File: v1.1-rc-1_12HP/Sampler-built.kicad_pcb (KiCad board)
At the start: 2 copper layers, 173.5 x 198.7 mm, 267 parts, among them J10 Eurorack_Power_10pin_Unshroud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, J11 3.5mm_Mono_Switched, J12 3.5mm_Mono_Switched, J13 3.5mm_Mono_Switched, J14 3.5mm_Mono_Switched, J15 3.5mm_Mono_Switched, J16 3.5mm_Mono_Switched, J17 3.5mm_Mono_Switched, J2 3.5mm_Mono_Switched, J3 Conn_01x04, J4 Conn_02x04, J6 3.5mm_Mono_Switched, J7 3.5mm_Mono_Switched, J8 3.5mm_Mono_Switched, J9 3.5mm_Mono_Switched, U1 TL072H, U10 TL072H, U11 TL072H, U12 TL072H, U13 AP62200WU-7, U15 NJM2068, U16 NJM2068, U17 AZ1117CR-3.3TRG1, U2 STM32F746IE, U3 TL072H, U4 SDRAM_IS42S16400J-6BLI-TR, U5 TL072H, U6 NCP51460SN33, U7 TL072H, U8 TL072H, U9 PCM3060PW, Y1 16MHz_18pF_FA238

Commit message: v1.1-rc1-12HP: part placement and routing ip
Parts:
- removed C16, C20: 10nF_0402_16V, 4ms_Capacitor:C_0402
- removed C89: 18pF_0603_50V, 4ms_Capacitor:C_0603
- removed C91, C92, C93, C94, C95, C96: 100nF_0402_16V, 4ms_Capacitor:C_0402
- removed D10, D11, D12, D13, D14, D18, D2, D27, D28, D30, D31, D32, D4, D5, D6, D8, D9: BAT54S, 4ms_Package_SOT:SOT23-3_PO132
- removed R31: 3k_0402, 4ms_Resistor:R_0402
- removed R37: 68Ω_0402, 4ms_Resistor:R_0402
- removed R38: 10k_0603, 4ms_Resistor:R_0603
- removed R39: 2k_0402, 4ms_Resistor:R_0402
- removed R69, R72: 1k_0603, 4ms_Resistor:R_0603
- removed R76: 47k_0603, 4ms_Resistor:R_0603
- removed S1, S2: SW_Push_PTS526 SM15 SMTR2 LFS, 4ms_Switch:Button_Tact_PTS526
- removed U17: AZ1117CR-3.3TRG1, 4ms_Package_SOT:SOT89-3
- removed U7: TL072H, 4ms_Package_SSOP:TSSOP-8_4.4x3mm_Pitch0.65mm
- added U14: TL072H, 4ms_Package_SSOP:TSSOP-8_4.4x3mm_Pitch0.65mm, F.Cu at (167.2, 66.8)
- C1, C10, C11, C13, C14, C17, C18, C3, C53, C7, C9: value 0.1uF_0603_16V -> 100nF_0402_16V; footprint 4ms_Capacitor:C_0603 -> 4ms_Capacitor:C_0402
- C12: value 100pF_0603_50V -> 100nF_0402_16V; footprint 4ms_Capacitor:C_0603 -> 4ms_Capacitor:C_0402
- C147, C148, C149, C150, C152, C153, C19, C34, C44, C45, C48, C52, C58, C59, C60, C61, C62, C63, C64, C67, C68, C69, C70, C71, C72, C73, C74, C75, C76, C77, C78, C8, C82, D1, D15, D22, D24, D26, D7, L1, R1, R10, R11, R12, R14, R152, R153, R157, R158, R159, R160, R161, R162, R163, R164, R18, R19, R2, R22, R23, R27, R28, R30, R33, R34, R40, R41, R42, R43, R44, R45, R46, R49, R50, R51, R52, R53, R54, R55, R6, R65, R66, R67, R7, U1, U10, U11, U12, U13, U3, U5, U8: moved to F.Cu
- C2: value 0.1uF_0603_16V -> 2.2uF_0603_25V
- C21, C24: value 100nF_0402_16V -> 47uF_5x5.3_16V; footprint 4ms_Capacitor:C_0402 -> 4ms_Capacitor:CP_Elec_5x5.3; moved to F.Cu
- C23: value 2.2uF_0603_25V -> 18pF_0603_50V
- C25, C26: value 2.2uF_0603_25V -> 0.1uF_0603_16V; moved to F.Cu
- C35, C37: value 100nF_0402_16V -> 100nF_0402_50V
- C38, C40: value 100nF_0402_16V -> 100nF_0402_50V; moved to F.Cu
- C39, C47: value 10nF_0402_16V -> 0.1uF_0603_16V; footprint 4ms_Capacitor:C_0402 -> 4ms_Capacitor:C_0603; moved to F.Cu
- C4, C5: value 47uF_5x5.3_16V -> 2.2uF_0603_25V; footprint 4ms_Capacitor:CP_Elec_5x5.3 -> 4ms_Capacitor:C_0603
- C42: value 100nF_0402_16V -> 0.1uF_0603_16V; footprint 4ms_Capacitor:C_0402 -> 4ms_Capacitor:C_0603; moved to F.Cu
- C43: value 1uF_0603_25V -> 4.7uF_1206_lowESR; footprint 4ms_Capacitor:C_0603 -> 4ms_Capacitor:C_1206
- C46: value 4.7uF_1206_lowESR -> 1nF_0603_50V; footprint 4ms_Capacitor:C_1206 -> 4ms_Capacitor:C_0603; moved to F.Cu
- C50: value 2.2uF_0603_25V -> 100nF_0402_16V; footprint 4ms_Capacitor:C_0603 -> 4ms_Capacitor:C_0402
- C6: value 1nF_0603_50V -> 100nF_0402_16V; footprint 4ms_Capacitor:C_0603 -> 4ms_Capacitor:C_0402
- C65, C66: value 100nF_0402_50V -> 0.1uF_0603_16V; footprint 4ms_Capacitor:C_0402 -> 4ms_Capacitor:C_0603; moved to F.Cu
- C79: value 100nF_0402_16V -> 0.1uF_0603_16V; footprint 4ms_Capacitor:C_0402 -> 4ms_Capacitor:C_0603
- C83: value 10nF_0402_16V -> 0.1uF_0603_16V; footprint 4ms_Capacitor:C_0402 -> 4ms_Capacitor:C_0603
- C84: value 10nF_0402_16V -> 100pF_0603_50V; footprint 4ms_Capacitor:C_0402 -> 4ms_Capacitor:C_0603
- C87, C88: value 10nF_0402_16V -> 100nF_0402_50V
- R13, R35, R5: value 2k_0402 -> 2k_0603; footprint 4ms_Resistor:R_0402 -> 4ms_Resistor:R_0603; moved to F.Cu
- R29: value 10k_0603 -> 20k_0603
- R3: value 2k_0402 -> 2k_0603; footprint 4ms_Resistor:R_0402 -> 4ms_Resistor:R_0603
- R36: value 10k_0402 -> 10k_0603; footprint 4ms_Resistor:R_0402 -> 4ms_Resistor:R_0603; moved to F.Cu
- R4: value 1k_0603 -> 3k_0402; footprint 4ms_Resistor:R_0603 -> 4ms_Resistor:R_0402
- R64, R68: value 1k_0603 -> 2k_0603
- R9: value 2k_0402 -> 1k_0603; footprint 4ms_Resistor:R_0402 -> 4ms_Resistor:R_0603; moved to F.Cu
- moved C90 250.7 mm to (169.5, 102.4)
- moved C57 247.6 mm to (163.1, 104.2), turned to 90 degrees
- moved R57 242.9 mm to (169.9, 83.1), turned to -90 degrees
- moved R56 242.6 mm to (169.9, 79.7), turned to -90 degrees
- moved R29 240.1 mm to (167.3, 82.1)
- moved C87 235.5 mm to (168.8, 64.2), turned to 180 degrees
- moved R32 234.5 mm to (164.4, 76.5)
- moved R60 234.1 mm to (148.8, 116.4), turned to -90 degrees
- moved C97 232.9 mm to (170.0, 69.9), turned to -90 degrees
- moved C88 231.3 mm to (165.8, 64.2)
- moved U15 231.2 mm to (165.0, 79.4)
- moved R61 230.9 mm to (148.8, 112.1), turned to 90 degrees
- moved C84 230.2 mm to (146.2, 112.5), turned to 180 degrees
- moved R63 229.7 mm to (143.6, 111.5), turned to 90 degrees
- moved R62 226.9 mm to (146.2, 110.8), turned to 180 degrees
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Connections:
- net +5VA renamed +5V
- net Net-(U2A-BOOT) renamed /BOOT0
- net Net-(U2A-NRST) renamed /NRST
- C1 pad 1: Net-(D9-AK) -> +3V3
- C1 pad 2: GNDADC -> GND
- C10 pad 1: +12V -> +3V3
- C11 pad 1: -12VA -> +3V3
- C12 pad 1: Net-(U16A--) -> +3V3
- C12 pad 2: Net-(C12-Pad2) -> GND
- C13 pad 1: +12V -> +3V3
- C14 pad 1: -12VA -> +3V3
- C17 pad 1: +12V -> +3V3
- C18 pad 1: -12VA -> +3V3
- C19 pad 1: Net-(D7-AK) -> /D2
- C2 pad 1: Net-(POT_SAMP1-Center) -> Net-(U2B-VCAP_2)
- C2 pad 2: GNDADC -> GND
- C21 pad 1: +3V3 -> +12V
- C23 pad 1: Net-(U2B-VCAP_2) -> /OSC_OUT
- C24 pad 1: +3V3 -> GND
- C24 pad 2: GND -> -12VA
- C25 pad 1: Net-(U2B-VCAP_1) -> +12V
- C26 pad 1: GND -> -12VA
- C26 pad 2: Net-(U2B-VDD12OTGHS) -> GND
- C27 pad 1: +3.3VADC -> +3V3
- C27 pad 2: GNDADC -> GND
- C3 pad 1: GND -> +3V3
- C3 pad 2: Net-(U15B-+) -> GND
- C35 pad 1: +3V3 -> +12V
- C37 pad 1: +3V3 -> -12VA
- C38 pad 1: +3V3 -> +12V
- C39 pad 1: Net-(D28-AK) -> /A6
- C4 pad 1: +12V -> Net-(U2B-VCAP_1)
- C40 pad 1: +3V3 -> -12VA
- C42 pad 1: +3V3 -> GND
- C42 pad 2: GND -> Net-(U15B-+)
- C43 pad 1: +12V -> +3V3
- C46 pad 1: +3V3 -> Net-(C46-Pad1)
- C46 pad 2: GND -> Net-(U15B--)
- C47 pad 1: Net-(D32-AK) -> /D6
- C5 pad 2: -12VA -> Net-(U2B-VDD12OTGHS)
- C53 pad 1: /D6 -> +3V3
- C54 pad 1: Net-(C54-Pad1) -> /D12
- C6 pad 1: Net-(C6-Pad1) -> +3.3VADC
- C6 pad 2: Net-(U15B--) -> GNDADC
- C65 pad 1: +12V -> Net-(POT_START1-Center)
- C65 pad 2: GND -> GNDADC
- C66 pad 1: -12VA -> Net-(POT_LENGTH1-Center)
- C66 pad 2: GND -> GNDADC
- C7 pad 1: Net-(POT_LENGTH1-Center) -> +3V3
- C7 pad 2: GNDADC -> GND
- C79 pad 1: +3V3 -> Net-(POT_SAMP1-Center)
- C79 pad 2: GND -> GNDADC
- C83 pad 1: Net-(Bank_But1-G) -> Net-(POT_PITCH1-Center)
- C83 pad 2: GND -> GNDADC
- C84 pad 1: Net-(D10-AK) -> Net-(U16B--)
- C84 pad 2: GND -> Net-(C84-Pad2)
- C87 pad 1: Net-(D18-AK) -> +12V
- C88 pad 1: Net-(D31-AK) -> -12VA
- C9 pad 1: Net-(POT_START1-Center) -> +3V3
- C9 pad 2: GNDADC -> GND
- D7 pad 3: Net-(D7-AK) -> /D2
- J13 pad 3: unconnected-(J13-SW-Pad3) -> GND
- J14 pad 3: unconnected-(J14-SW-Pad3) -> GND
- J4 pad 1: unconnected-(J4-Pin_1-Pad1) -> /UART_TX
- J4 pad 2: unconnected-(J4-Pin_2-Pad2) -> GND
- J4 pad 3: unconnected-(J4-Pin_3-Pad3) -> /UART_RX
- J4 pad 4: unconnected-(J4-Pin_4-Pad4) -> GND
- J4 pad 5: unconnected-(J4-Pin_5-Pad5) -> /DEBUG2
- J4 pad 6: unconnected-(J4-Pin_6-Pad6) -> GND
- J4 pad 7: unconnected-(J4-Pin_7-Pad7) -> /DEBUG3
- J4 pad 8: unconnected-(J4-Pin_8-Pad8) -> GND
- POT_PITCH1 pad 2: Net-(D9-AK) -> Net-(POT_PITCH1-Center)
- R1 pad 1: /A0 -> Net-(R1-Pad1)
- R11 pad 1: /A1 -> Net-(POT_PITCH1-Center)
- R11 pad 2: Net-(D9-AK) -> Net-(U1B-+)
- R12 pad 2: Net-(D9-AK) -> /A1
- R13 pad 2: Net-(D10-AK) -> Net-(REV_BUT1-B)
- R15 pad 2: Net-(D1-AK) -> Net-(R1-Pad1)
- R17 pad 1: Net-(J7-SIG) -> Net-(J9-SIG)
- R18 pad 1: /A2 -> Net-(C46-Pad1)
- R19 pad 1: Net-(U3A--) -> Net-(U14B--)
- R19 pad 2: Net-(C6-Pad1) -> /A2
- R2 pad 1: Net-(U1A--) -> Net-(U10A--)
- R2 pad 2: Net-(D1-AK) -> /A0
- R20 pad 1: Net-(J9-SIG) -> Net-(J7-SIG)
- R21 pad 2: Net-(D1-AK) -> Net-(R1-Pad1)
- R22 pad 1: /A3 -> Net-(POT_LENGTH1-Center)
- R22 pad 2: Net-(D18-AK) -> Net-(U3B-+)
- R23 pad 2: Net-(POT_START1-Center) -> /A3
- R27 pad 1: /A4 -> Net-(R20-Pad2)
- R28 pad 2: Net-(R20-Pad2) -> /A4
- R29 pad 2: Net-(R29-Pad2) -> Net-(U15B-+)
- R30 pad 1: /A5 -> Net-(R16-Pad2)
- R33 pad 1: /A8 -> Net-(R17-Pad2)
- R34 pad 1: Net-(U7A--) -> Net-(U5B--)
- R34 pad 2: Net-(R17-Pad2) -> /A8
- R36 pad 2: Net-(D28-AK) -> Net-(REV_BUT1-POLE-A)
- R4 pad 1: Net-(J8-SIG) -> GND
- R4 pad 2: Net-(U15A-+) -> Net-(U2B-OTG_HR_REXT)
- R40 pad 1: /A7 -> Net-(POT_START1-Center)
- R40 pad 2: Net-(D31-AK) -> Net-(U1A-+)
- R41 pad 1: Net-(U10A--) -> Net-(U1A--)
- R41 pad 2: Net-(POT_LENGTH1-Center) -> /A7
- R45 pad 1: /A9 -> Net-(POT_SAMP1-Center)
- R45 pad 2: Net-(D32-AK) -> Net-(U3A-+)
- R46 pad 1: Net-(U10B--) -> Net-(U3A--)
- R46 pad 2: Net-(POT_SAMP1-Center) -> /A9
- R56 pad 1: Net-(C6-Pad1) -> Net-(C46-Pad1)
- R58 pad 2: Net-(D7-AK) -> /D2
- R60 pad 2: Net-(U16A-+) -> Net-(U16B-+)
- R61 pad 2: Net-(U16A--) -> Net-(U16B--)
- R62 pad 1: Net-(U16A--) -> Net-(U16B--)
- R62 pad 2: Net-(C12-Pad2) -> Net-(C84-Pad2)
- R63 pad 1: Net-(C12-Pad2) -> Net-(C84-Pad2)
- R64 pad 2: Net-(R64-Pad2) -> Net-(Bank_But1-B)
- R68 pad 2: Net-(R68-Pad2) -> Net-(REV_BUT1-R)
- R74 pad 2: Net-(C54-Pad1) -> /D12
- R81 pad 1: Net-(U5B--) -> Net-(U10B--)
- R81 pad 2: Net-(R16-Pad2) -> /A5
- R9 pad 1: /D2 -> Net-(J8-SIG)
- R9 pad 2: Net-(D7-AK) -> Net-(U15A-+)
- REV_BUT1 pad 8: Net-(D10-AK) -> Net-(REV_BUT1-B)
- U1 pad 3: Net-(D1-AK) -> Net-(U1A-+)
- U1 pad 5: Net-(D9-AK) -> Net-(U1B-+)
- U10 pad 3: Net-(D31-AK) -> Net-(D1-AK)
- U10 pad 5: Net-(D32-AK) -> Net-(D24-AK)
- U15 pad 7: Net-(C6-Pad1) -> Net-(C46-Pad1)
- U16 pad 1: Net-(C12-Pad2) -> Net-(U16A--)
- U16 pad 3: Net-(U16A-+) -> GND
- U16 pad 5: GND -> Net-(U16B-+)
- U16 pad 7: Net-(U16B--) -> Net-(C84-Pad2)
- U2 pad B15: /USB_DP -> unconnected-(U2A-PA12-PadB15)
- U2 pad C15: /USB_DM -> unconnected-(U2A-PA11-PadC15)
- U2 pad D15: /USB_ID -> unconnected-(U2A-PA10-PadD15)
- U2 pad E15: /USB_VBUS -> unconnected-(U2A-PA9-PadE15)
- U3 pad 3: Net-(D15-AK) -> Net-(U3A-+)
- U3 pad 5: Net-(D18-AK) -> Net-(U3B-+)
- U5 pad 5: Net-(D24-AK) -> Net-(D26-AK)
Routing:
- net (no net): track 438.9 -> 2.96 mm, vias 48 -> 2
- net GND: track 391.8 -> 159.6 mm, vias 62 -> 31
- net +12V: track 193.2 -> 24.3 mm, vias 19 -> 1
- net -12VA: track 165.3 -> 5.12 mm, vias 15 -> 2
- net Net-(D9-AK): track 106.7 -> 0.00 mm, vias 8 -> 0
- net Net-(D1-AK): track 106.5 -> 0.00 mm, vias 2 -> 0
- net VREF+: track 103.6 -> 5.32 mm, vias 8 -> 2
- net GNDADC: track 70.2 -> 5.26 mm, vias 5 -> 0
- net /UART_TX: track 66.2 -> 2.96 mm, vias 5 -> 0
- net /A6: track 64.2 -> 11.1 mm, vias 6 -> 3
- net /D16: track 57.5 -> 9.02 mm, vias 4 -> 1
- net /SD-NE1: track 0.00 -> 48.3 mm, vias 0 -> 4
- net Net-(C6-Pad1): track 44.8 -> 0.00 mm, vias 5 -> 0
- net /D13: track 61.2 -> 17.0 mm, vias 6 -> 4
- net /D3: track 51.5 -> 7.84 mm, vias 6 -> 2
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- added copper zone on In2.Cu, net +3V3
- added copper zone on In1.Cu, net GND
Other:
- board size 173.5 x 198.7 mm -> 221.7 x 109.2 mm
- copper layers 2 -> 4
- board text added: "D11"
- board text added: "D27"
- board text added: "U13"
- board text removed: "1"
- board text removed: "A0"
- board text removed: "A1"
- board text removed: "ADC"
- board text removed: "BANK CV"
- board text removed: "BANK_CV"
- board text removed: "DAC"
- board text removed: "END OUT"
- board text removed: "END_OUT"
- board text removed: "GND"
- board text removed: "IN L"
- board text removed: "IN R"
- board text removed: "IN_L"
- board text removed: "IN_R"
- board text removed: "LEN CV"
- board text removed: "LENGTH_CV"
- board text removed: "OUT L"
- board text removed: "OUT R"
- board text removed: "OUT_L"
- board text removed: "OUT_R"
- board text removed: "PITCH CV"
- board text removed: "PITCH_CV"
- board text removed: "PLAY_TRIG"
- board text removed: "RESET"
- board text removed: "REV TRIG"
- board text removed: "REV_TRIG"
- board text removed: "SAMP CV"
- board text removed: "SAMP_CV"
- board text removed: "START CV"
- board text removed: "START_CV"
- board text removed: "SWD"
- board text removed: "TX"

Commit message: v1.1 rc1 12hp: routing IP
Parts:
- moved J3 55.7 mm to (174.1, 45.3)
- moved C67 13.7 mm to (126.3, 67.0), turned to 90 degrees
- moved R42 11.5 mm to (173.2, 104.8), turned to -90 degrees
- moved R41 11.1 mm to (170.8, 62.4), turned to 180 degrees
- moved R66 10.8 mm to (128.7, 68.9), turned to 0 degrees
- moved C59 10.5 mm to (164.8, 62.3), turned to 0 degrees
- moved R44 10.4 mm to (162.4, 103.5), turned to 90 degrees
- moved R49 10.2 mm to (162.4, 105.5), turned to -90 degrees
- moved C60 10.0 mm to (168.4, 62.3), turned to 180 degrees
- moved R55 9.60 mm to (172.0, 103.2), turned to 180 degrees
- moved R12 9.29 mm to (162.8, 60.0), turned to 180 degrees
- moved U13 8.87 mm to (129.7, 66.6), turned to 0 degrees
- moved C57 8.73 mm to (171.8, 105.4), turned to -90 degrees
- moved R40 8.60 mm to (172.3, 58.7), turned to -90 degrees
- moved R11 8.12 mm to (162.7, 58.7), turned to 0 degrees
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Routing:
- net +12V: track 24.3 -> 260.5 mm, vias 1 -> 19
- net -12VA: track 5.12 -> 220.5 mm, vias 2 -> 12
- net +3V3: track 157.7 -> 368.6 mm, vias 22 -> 24
- net GND: track 159.6 -> 323.2 mm, vias 31 -> 45
- net VREF+: track 5.32 -> 146.6 mm
- net GNDADC: track 5.26 -> 143.2 mm, vias 0 -> 4
- net /D2: track 5.62 -> 85.9 mm, vias 2 -> 4
- net /D10: track 7.87 -> 86.9 mm, vias 0 -> 2
- net /SAI_FS: track 3.19 -> 75.9 mm, vias 1 -> 4
- net /CODEC_RESET: track 3.13 -> 73.4 mm, vias 1 -> 2
- net /D7: track 28.3 -> 95.9 mm, vias 3 -> 4
- net /SAI_SCK: track 4.87 -> 71.1 mm, vias 1 -> 4
- net /SAI_SD_B: track 3.06 -> 69.0 mm, vias 1 -> 4
- net /SAI_MCLK: track 4.09 -> 68.9 mm, vias 1 -> 4
- net /D8: track 28.9 -> 92.9 mm, vias 2 -> 4
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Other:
- board size 221.7 x 109.2 mm -> 221.7 x 109.7 mm

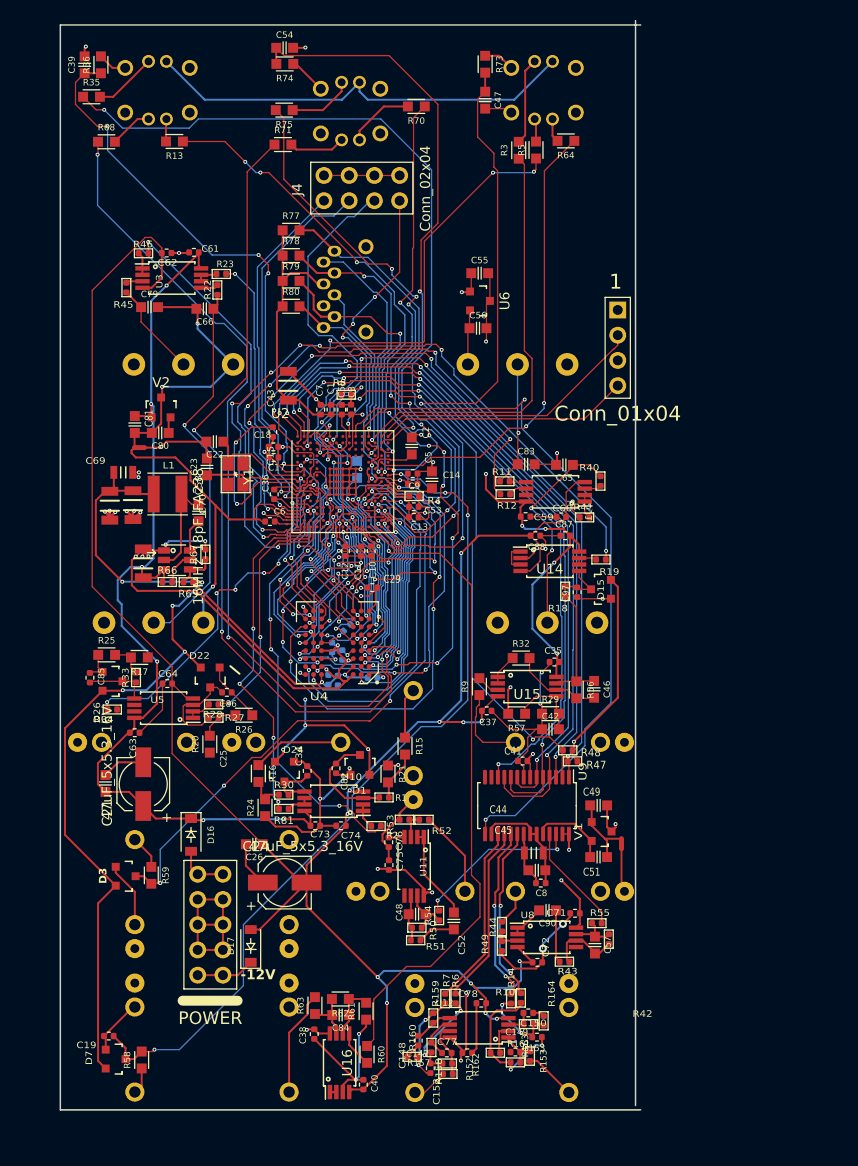
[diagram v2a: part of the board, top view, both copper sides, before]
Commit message: v1.1-rc1-12HP: finished routing and silk
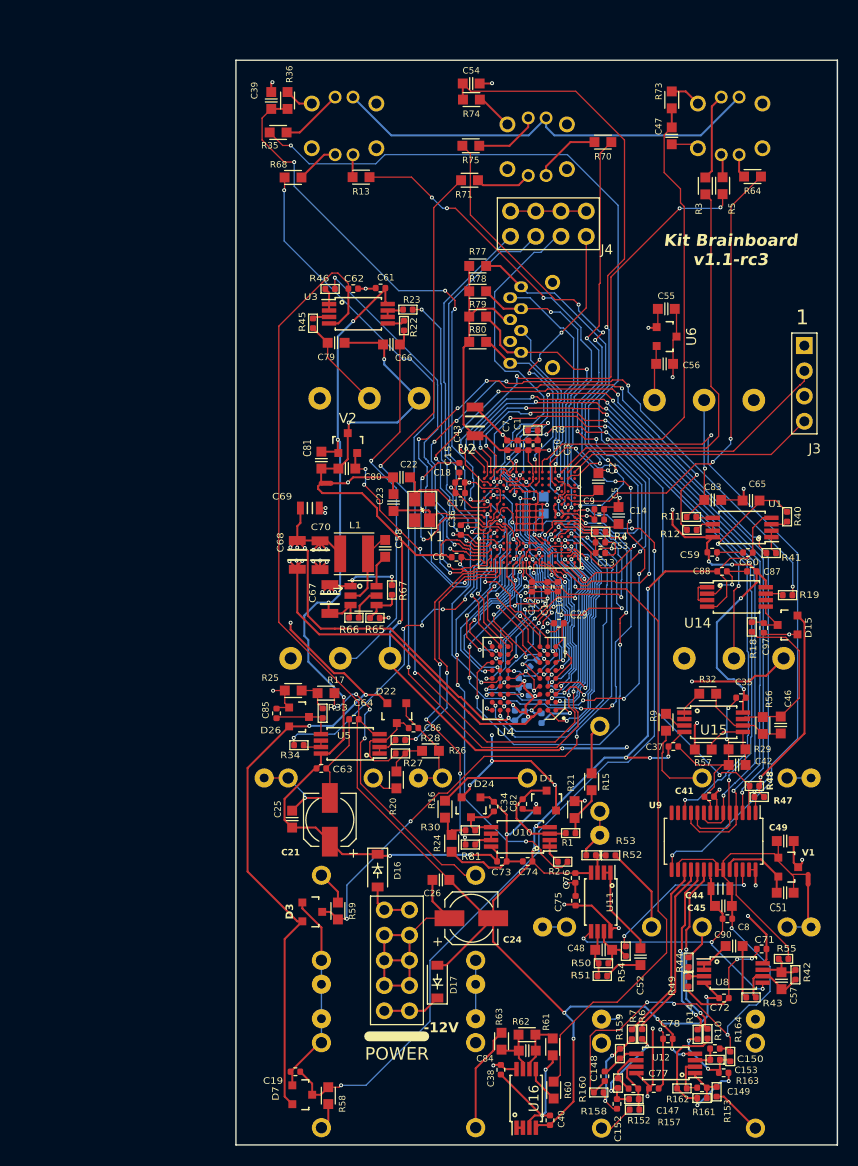
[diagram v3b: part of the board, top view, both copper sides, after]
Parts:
- moved L1 19.7 mm to (147.5, 66.0)
- moved C68 19.5 mm to (141.8, 66.1)
- moved C70 19.5 mm to (144.1, 66.2)
- moved C11 19.1 mm to (167.0, 69.3)
- moved C12 19.1 mm to (165.5, 69.3)
- moved C14 19.1 mm to (172.2, 61.5)
- moved C148 19.1 mm to (172.8, 118.6)
- moved C17 19.1 mm to (158.2, 59.9)
- moved C18 19.1 mm to (158.2, 58.8)
- moved C19 19.1 mm to (141.6, 118.2)
- moved C2 19.1 mm to (172.1, 58.8)
- moved C21 19.1 mm to (145.1, 92.8)
- moved C23 19.1 mm to (151.5, 60.9)
- moved C27 19.1 mm to (165.6, 77.0)
- moved C29 19.1 mm to (168.2, 73.0)
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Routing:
- net GND: track 323.2 -> 375.2 mm, vias 45 -> 53
- net GNDA: track 21.3 -> 65.9 mm, vias 0 -> 4
- net Net-(J9-SIG): track 0.00 -> 29.5 mm, vias 0 -> 4
- net /SD-NBL0: track 0.00 -> 26.7 mm, vias 0 -> 2
- net /VCOM: track 4.88 -> 29.7 mm, vias 0 -> 3
- net +3.3VADC: track 3.76 -> 25.3 mm, vias 0 -> 4
- net VREF+: track 146.6 -> 158.4 mm
- net +3V3: track 368.6 -> 374.1 mm, vias 24 -> 29
- net -12VA: track 220.5 -> 225.2 mm
- net Net-(C46-Pad1): track 12.9 -> 16.8 mm
- net Net-(J7-SIG): track 0.00 -> 2.77 mm
- net Net-(U13-SW): track 9.99 -> 7.38 mm
- net Net-(U5B--): track 0.00 -> 2.19 mm
- net Net-(U12A--): track 3.02 -> 4.00 mm
- net /A4: track 23.9 -> 24.4 mm
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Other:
- board size 221.7 x 109.7 mm -> 241.5 x 109.2 mm
- board text removed: "D11"
- board text removed: "D27"
- board text removed: "U13"
- board text removed: "USB BOOT"

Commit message: Removed extra EdgeCuts line
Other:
- board size 241.5 x 109.2 mm -> 60.5 x 109.2 mm

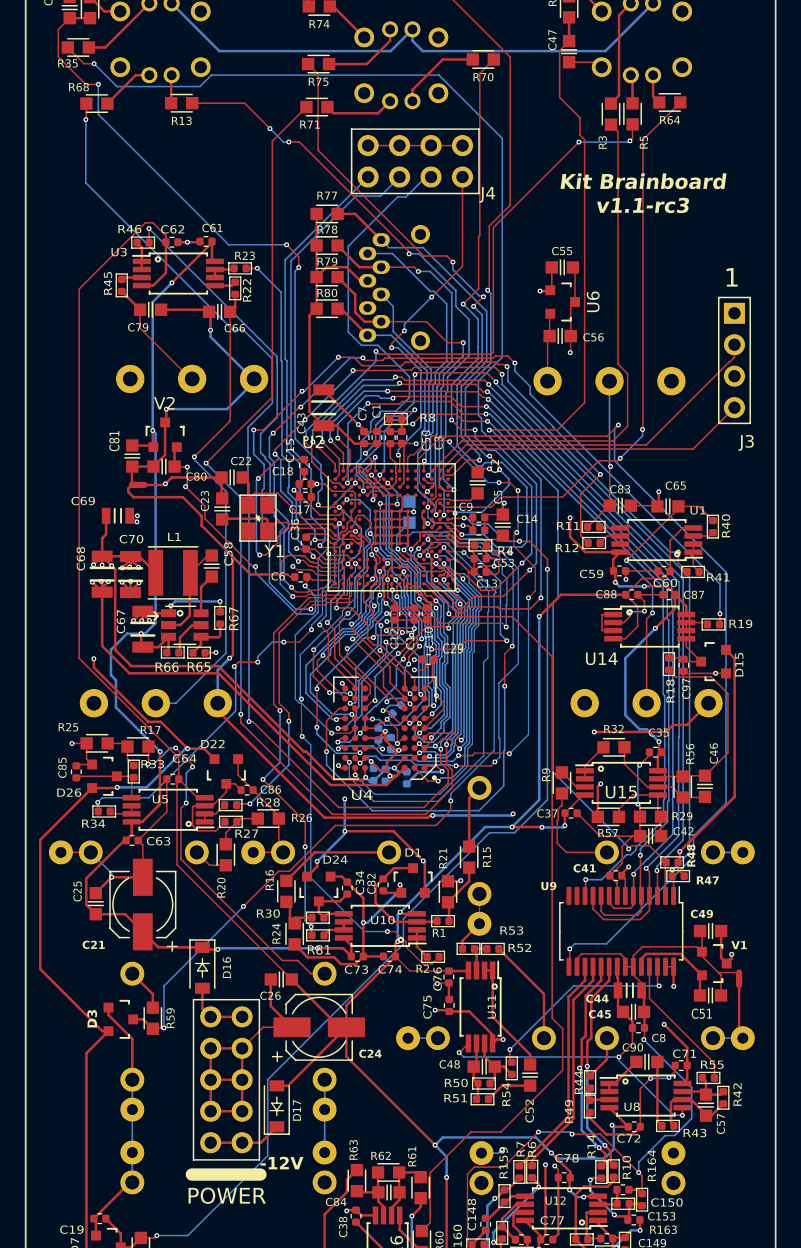
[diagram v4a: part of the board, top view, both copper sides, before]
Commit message: Re-routing in progress
TODO:
- A2 (PitchCV) on red layer, routing CCW from ARM pin to opamp, avoiding digital lines
- Put SAI/I2C traces that are north of ARM => to orange layer
- Put digital red traces in the area under the START1_POT => to blue/orange layer
- Move VREF/GNDADC to red layer (might need to go to orange layer when crossing board east->west
- Move U6 to near V2, using the nettie for GNDADC-GND for U6
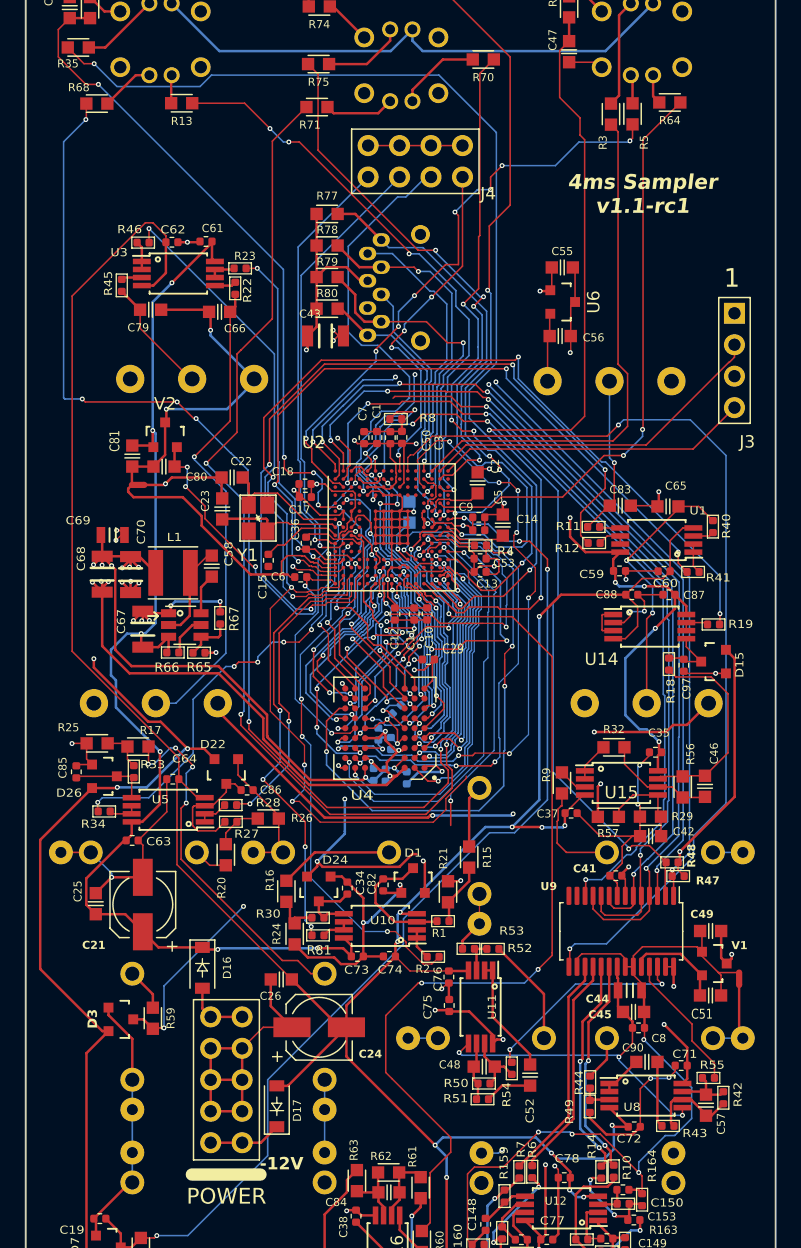
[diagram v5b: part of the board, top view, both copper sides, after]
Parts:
- moved C15 8.19 mm to (155.2, 65.0)
- moved C43 5.80 mm to (159.9, 46.9), turned to 0 degrees
- moved C69 1.61 mm to (142.7, 63.0)
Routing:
- net /A2: track 69.4 -> 107.7 mm
- net GNDADC: track 142.8 -> 173.4 mm, vias 7 -> 6
- net +12V: track 261.0 -> 241.0 mm
- net /D13: track 63.0 -> 44.3 mm
- net /NRST: track 18.2 -> 6.51 mm, vias 2 -> 0
- net +3V3: track 374.1 -> 366.5 mm, vias 29 -> 30
- net /D15: track 69.8 -> 77.0 mm, vias 2 -> 4
- net /D7: track 95.9 -> 100.9 mm, vias 4 -> 7
- net /CODEC_RESET: track 73.4 -> 77.2 mm
- net GND: track 375.2 -> 372.5 mm, vias 53 -> 54
- net /UART_RX: track 37.9 -> 35.8 mm
- net /D1: track 49.9 -> 48.1 mm, vias 4 -> 8
- net /A6: track 61.9 -> 60.2 mm
- net /A7: track 58.1 -> 59.3 mm, vias 6 -> 4
- net VREF+: track 158.4 -> 159.5 mm
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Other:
- board text added: "4ms Sampler v1.1-rc1"
- board text removed: "Kit Brainboard v1.1-rc3"
